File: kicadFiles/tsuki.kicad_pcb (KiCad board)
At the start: 2 copper layers, 283 x 94.2 mm, 392 parts, among them J1 TYPE-C-31-M12_13, J2 Conn_01x12, J3 Conn_ARM_JTAG_SWD_10, Q1 BSS138, Q2 AO4407A, SW1 ESC, SW10 9, SW11 0, SW12 -_, SW13 +=, SW14 2U BKSP, SW15 TAB_150, SW16 Q, SW17 W, SW18 E, SW19 R, SW2 1, SW20 T, SW21 Y, SW22 U, SW23 I, SW24 O, SW25 P, SW26 [{, SW27 ]}, SW28 \|_150, SW29 CAPS_175, SW3 2, SW30 A, SW31 S, SW32 D, SW33 F, SW34 G, SW35 H, SW36 J, SW37 K, SW38 L, SW39 :;, SW4 3, SW40 "', SW41 ENTER_225, SW42 LSHIFT_225, SW43 Z, SW44 X, SW45 C, SW46 V, SW47 B, SW48 N, SW49 M, SW5 4, SW50 <,, SW51 >., SW52 ?/, SW53 RSHIFT_275, SW54 LCTRL_150, SW55 LGUI_100, SW56 LALT_150, SW58 RALT_150, SW59 RGUI_150, SW6 5, SW60 RCTRL_150, SW61 FN_100, SW62 RSHIFT_175, SW63 STEPPED_CAPS_125, SW64 1U LBKSP, SW65 1U RBKSP, SW66 ISO_100, SW67 ISO_ENTER, SW68 LCTRL_125, SW69 LGUI_125, SW7 6, SW70 LGUI_100, SW71 LALT_125, SW72 LALT_150, SW75 SPACE_625, SW77 SPACE_700, SW8 7, SW80 RALT_125, SW81 RALT_150, SW83 RGUI_125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

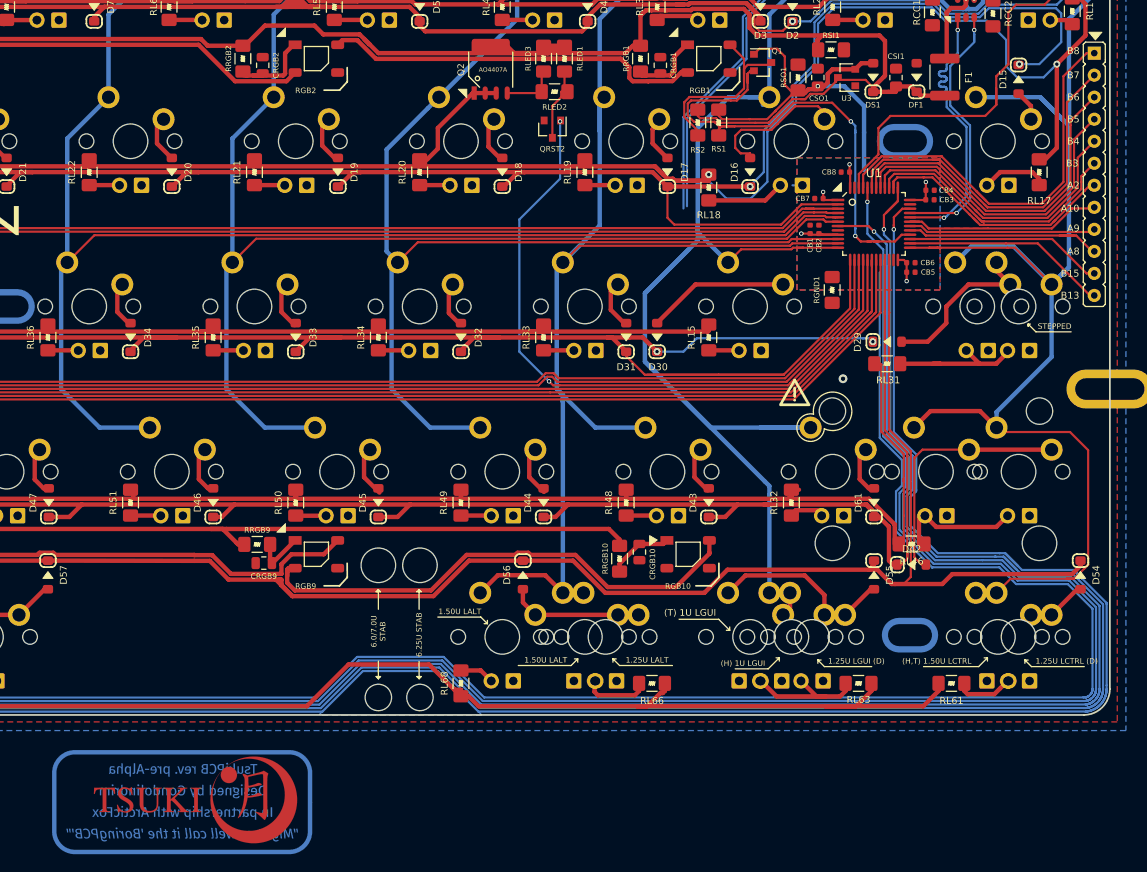
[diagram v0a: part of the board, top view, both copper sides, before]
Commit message: Add rotary encoder support
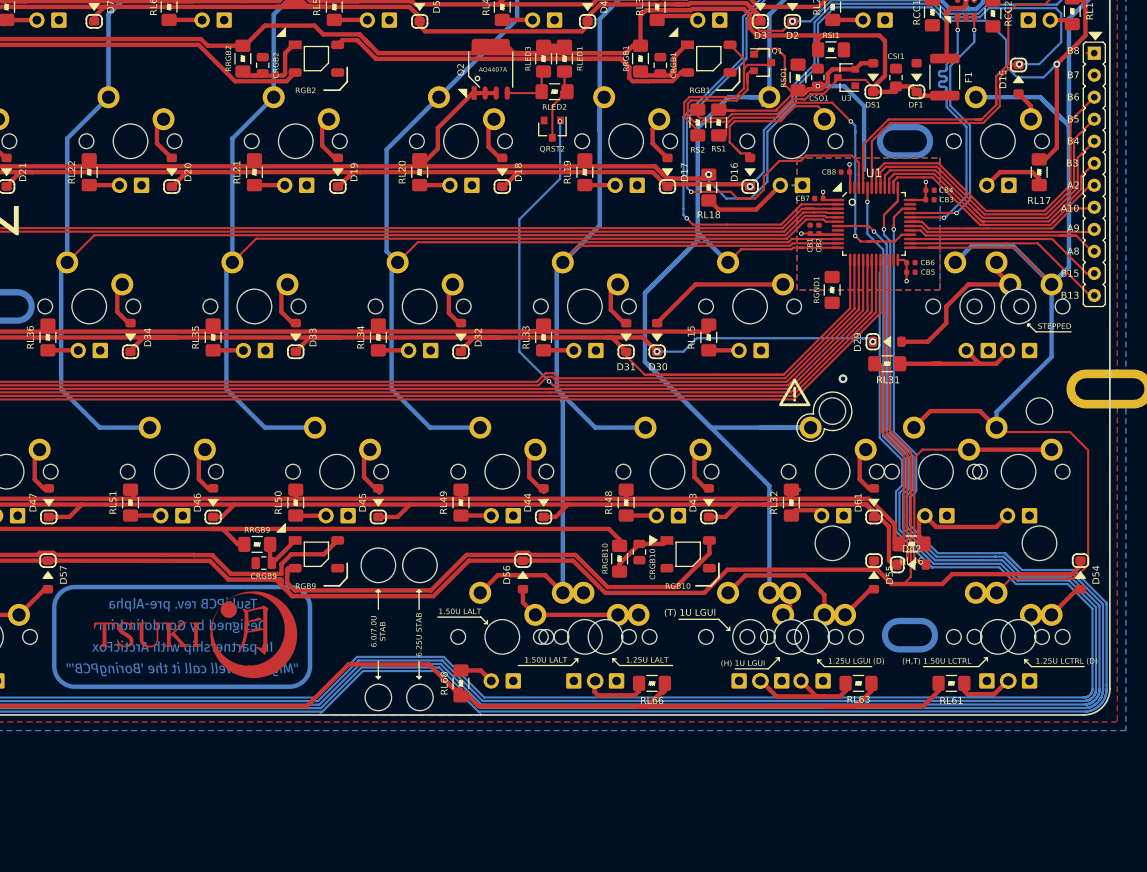
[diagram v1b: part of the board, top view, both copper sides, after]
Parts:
- moved L1 19.1 mm to (248.9, 167.3)
- moved L4 19.1 mm to (247.4, 167.6)
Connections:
- U1 pad 2: Row2 -> ENC_B
- U1 pad 43: Extra2 -> Row2
- U1 pad 45: Extra1 -> Row1
- U1 pad 46: Row1 -> ENC_A
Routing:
- net Extra1: track 47.9 -> 1.52 mm
- net Extra2: track 43.5 -> 0.00 mm
- net ENC_A: track 301.8 -> 326.3 mm, vias 1 -> 2
- net ENC_B: track 305.1 -> 325.1 mm, vias 1 -> 2
- net Row2: track 367.6 -> 371.7 mm
- net Net-(Q2-Pad1): track 1668.3 -> 1664.5 mm
- net Net-(D16-Pad2): track 16.6 -> 19.7 mm
- net RGB_3V3: track 59.4 -> 57.2 mm
- net Net-(LED18-PadA): track 8.98 -> 9.85 mm
- net Row1: track 360.0 -> 360.6 mm
- net 3.3V: track 464.3 -> 464.8 mm

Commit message: Refreshed renders and KLE
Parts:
- removed D66: 1N4148, acheron_Components:D_SOD-123
- removed LED67, LED70: LED, acheron_Components:LED_THT_2.54mm
- removed RL68: 420R, acheron_Components:R_SMD_1206
- removed SW55: LGUI_100, acheron_MX_SolderMask:MX150
- removed SW56: LALT_150, acheron_MX_SolderMask:MX150
- added D63: 1N4148, acheron_Components:D_SOD-123, F.Cu at (117.6, 166.4)
- SW59: value RGUI_150 -> RGUI_100; footprint acheron_MX_SolderMask:MX150 -> acheron_MX_SolderMask:MX100
- moved D59 35.7 mm to (134.2, 160.4)
- moved RLED3 15.3 mm to (273.9, 98.7), turned to 180 degrees
- moved LED77 14.3 mm to (127.1, 172.6)
- moved SW59 14.3 mm to (127.1, 167.6)
- moved RLED2 12.2 mm to (278.9, 100.6), turned to 270 degrees
- moved LED74 9.52 mm to (150.9, 172.6), turned to 180 degrees
- moved SW58 9.52 mm to (150.9, 167.6)
- moved D58 9.52 mm to (143.8, 160.4)
- moved RL71 5.76 mm to (141.6, 173.5)
- moved RL73 5.62 mm to (118.0, 172.8), turned to 270 degrees
- moved L2 3.34 mm to (158.9, 121.7)
- moved RL75 2.73 mm to (115.5, 172.8), turned to 270 degrees
- moved RLED1 2.51 mm to (289.0, 100.5)
- moved LED66 2.38 mm to (317.6, 172.6), turned to 180 degrees
- moved L3 1.09 mm to (208.5, 120.4)
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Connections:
- D58 pad 2: L7 -> L6
- D59 pad 2: L8 -> L7
- LED77 pad A: Net-(LED77-PadA) -> Net-(LED75-PadA)
- LED78 pad A: Net-(LED77-PadA) -> Net-(LED78-PadA)
- LED79 pad A: Net-(LED77-PadA) -> Net-(LED78-PadA)
- Q2 pad 1: Net-(Q2-Pad1) -> 5V
- Q2 pad 2: Net-(Q2-Pad1) -> 5V
- Q2 pad 3: Net-(Q2-Pad1) -> 5V
- Q2 pad 5: 5V -> Net-(Q2-Pad5)
- Q2 pad 6: 5V -> Net-(Q2-Pad5)
- Q2 pad 7: 5V -> Net-(Q2-Pad5)
- Q2 pad 8: 5V -> Net-(Q2-Pad5)
- RL1 pad 2: Net-(Q2-Pad1) -> Net-(Q2-Pad5)
- RL10 pad 2: Net-(Q2-Pad1) -> Net-(Q2-Pad5)
- RL11 pad 2: Net-(Q2-Pad1) -> Net-(Q2-Pad5)
- RL12 pad 2: Net-(Q2-Pad1) -> Net-(Q2-Pad5)
- RL13 pad 2: Net-(Q2-Pad1) -> Net-(Q2-Pad5)
- RL14 pad 2: Net-(Q2-Pad1) -> Net-(Q2-Pad5)
- RL15 pad 2: Net-(Q2-Pad1) -> Net-(Q2-Pad5)
- RL16 pad 2: Net-(Q2-Pad1) -> Net-(Q2-Pad5)
- RL17 pad 2: Net-(Q2-Pad1) -> Net-(Q2-Pad5)
- RL18 pad 2: Net-(Q2-Pad1) -> Net-(Q2-Pad5)
- RL19 pad 2: Net-(Q2-Pad1) -> Net-(Q2-Pad5)
- RL2 pad 2: Net-(Q2-Pad1) -> Net-(Q2-Pad5)
- RL20 pad 2: Net-(Q2-Pad1) -> Net-(Q2-Pad5)
- RL21 pad 2: Net-(Q2-Pad1) -> Net-(Q2-Pad5)
- RL22 pad 2: Net-(Q2-Pad1) -> Net-(Q2-Pad5)
- RL23 pad 2: Net-(Q2-Pad1) -> Net-(Q2-Pad5)
- RL24 pad 2: Net-(Q2-Pad1) -> Net-(Q2-Pad5)
- RL25 pad 2: Net-(Q2-Pad1) -> Net-(Q2-Pad5)
- RL26 pad 2: Net-(Q2-Pad1) -> Net-(Q2-Pad5)
- RL27 pad 2: Net-(Q2-Pad1) -> Net-(Q2-Pad5)
- RL28 pad 2: Net-(Q2-Pad1) -> Net-(Q2-Pad5)
- RL29 pad 2: Net-(Q2-Pad1) -> Net-(Q2-Pad5)
- RL3 pad 2: Net-(Q2-Pad1) -> Net-(Q2-Pad5)
- RL30 pad 2: Net-(Q2-Pad1) -> Net-(Q2-Pad5)
- RL31 pad 2: Net-(Q2-Pad1) -> Net-(Q2-Pad5)
- RL32 pad 2: Net-(Q2-Pad1) -> Net-(Q2-Pad5)
- RL33 pad 2: Net-(Q2-Pad1) -> Net-(Q2-Pad5)
- RL34 pad 2: Net-(Q2-Pad1) -> Net-(Q2-Pad5)
- RL35 pad 2: Net-(Q2-Pad1) -> Net-(Q2-Pad5)
- RL36 pad 2: Net-(Q2-Pad1) -> Net-(Q2-Pad5)
- RL37 pad 2: Net-(Q2-Pad1) -> Net-(Q2-Pad5)
- RL38 pad 2: Net-(Q2-Pad1) -> Net-(Q2-Pad5)
- RL39 pad 2: Net-(Q2-Pad1) -> Net-(Q2-Pad5)
- RL4 pad 2: Net-(Q2-Pad1) -> Net-(Q2-Pad5)
- RL40 pad 2: Net-(Q2-Pad1) -> Net-(Q2-Pad5)
- RL41 pad 2: Net-(Q2-Pad1) -> Net-(Q2-Pad5)
- RL42 pad 2: Net-(Q2-Pad1) -> Net-(Q2-Pad5)
- RL43 pad 2: Net-(Q2-Pad1) -> Net-(Q2-Pad5)
- RL44 pad 2: Net-(Q2-Pad1) -> Net-(Q2-Pad5)
- RL45 pad 2: Net-(Q2-Pad1) -> Net-(Q2-Pad5)
- RL46 pad 2: Net-(Q2-Pad1) -> Net-(Q2-Pad5)
- RL48 pad 2: Net-(Q2-Pad1) -> Net-(Q2-Pad5)
- RL49 pad 2: Net-(Q2-Pad1) -> Net-(Q2-Pad5)
- RL5 pad 2: Net-(Q2-Pad1) -> Net-(Q2-Pad5)
- RL50 pad 2: Net-(Q2-Pad1) -> Net-(Q2-Pad5)
- RL51 pad 2: Net-(Q2-Pad1) -> Net-(Q2-Pad5)
- RL52 pad 2: Net-(Q2-Pad1) -> Net-(Q2-Pad5)
- RL53 pad 2: Net-(Q2-Pad1) -> Net-(Q2-Pad5)
- RL54 pad 2: Net-(Q2-Pad1) -> Net-(Q2-Pad5)
- RL55 pad 2: Net-(Q2-Pad1) -> Net-(Q2-Pad5)
- RL56 pad 2: Net-(Q2-Pad1) -> Net-(Q2-Pad5)
- RL57 pad 2: Net-(Q2-Pad1) -> Net-(Q2-Pad5)
- RL58 pad 2: Net-(Q2-Pad1) -> Net-(Q2-Pad5)
- RL6 pad 2: Net-(Q2-Pad1) -> Net-(Q2-Pad5)
- RL60 pad 2: Net-(Q2-Pad1) -> Net-(Q2-Pad5)
- RL61 pad 2: Net-(Q2-Pad1) -> Net-(Q2-Pad5)
- RL63 pad 2: Net-(Q2-Pad1) -> Net-(Q2-Pad5)
- RL66 pad 2: Net-(Q2-Pad1) -> Net-(Q2-Pad5)
- RL69 pad 2: Net-(Q2-Pad1) -> Net-(Q2-Pad5)
- RL7 pad 2: Net-(Q2-Pad1) -> Net-(Q2-Pad5)
- RL71 pad 2: Net-(Q2-Pad1) -> Net-(Q2-Pad5)
- RL73 pad 2: Net-(Q2-Pad1) -> Net-(Q2-Pad5)
- RL75 pad 1: Net-(LED77-PadA) -> Net-(LED78-PadA)
- RL75 pad 2: Net-(Q2-Pad1) -> Net-(Q2-Pad5)
- RL77 pad 2: Net-(Q2-Pad1) -> Net-(Q2-Pad5)
- RL8 pad 2: Net-(Q2-Pad1) -> Net-(Q2-Pad5)
- RL9 pad 2: Net-(Q2-Pad1) -> Net-(Q2-Pad5)
- SW58 pad 1: Col11 -> Col10
- SW58 pad 2: L7 -> L6
- SW59 pad 1: L8 -> Col11
- SW59 pad 2: Col12 -> L7
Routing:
- net Net-(Q2-Pad1): track 1664.5 -> 0.00 mm, vias 2 -> 0
- net Net-(Q2-Pad5): track 0.00 -> 1653.5 mm, vias 0 -> 2
- net Net-(LED77-PadA): track 16.2 -> 0.00 mm
- net L2: track 22.1 -> 6.94 mm
- net Col3: track 145.4 -> 134.2 mm
- net Net-(QRST2-Pad3): track 8.92 -> 18.5 mm
- net Net-(LED78-PadA): track 0.00 -> 9.34 mm
- net Net-(LED65-PadA): track 15.2 -> 7.01 mm
- net Net-(LED75-PadA): track 7.71 -> 15.3 mm
- net L8: track 16.2 -> 8.78 mm
- net Net-(LED73-PadA): track 17.5 -> 10.3 mm
- net L7: track 15.3 -> 10.5 mm
- net L6: track 12.5 -> 16.9 mm
- net Net-(LED70-PadA): track 3.99 -> 0.00 mm
- net Row5: track 327.0 -> 330.5 mm
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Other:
- board text added: "(H) 1U RGUI"
- board text added: "(H,T) 1.50U LALT"
- board text added: "(H,T) 1U LGUI"
- board text added: "(IV) For detailed information, check the Acheron Docs page for the ArcticPCB: http://gondolindrim.github.io/AcheronDocs/tsuki/intro.html"
- board text added: "(T) 1.50U LCTRL"
- board text added: "- TsukiPCB's GitHub page: http://github.com/Gondolindrim/TsukiPCB"
- board text added: "1.50U RALT (T)"
- board text removed: "(H) 1U LGUI"
- board text removed: "(H,T) 1.50U LCTRL"
- board text removed: "(IV) For detailed information, check the Acheron Docs page for the ArcticPCB: http://gondolindrim.github.io/AcheronDocs/arctic/intro.html"
- board text removed: "(T) 1.50U RALT"
- board text removed: "(T) 1U LGUI"
- board text removed: "- ArcticPCB's GitHub page: http://github.com/Gondolindrim/ArcticPCB"
- board text removed: "1.50U LALT"
- board text removed: "1.50U RGUI (H)"

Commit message: Further adjust schematic
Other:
- board text removed: "(vi) Some switch fooprints had to be"
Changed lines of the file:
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@@
   (general
     (thickness 1.6)
-    (drawings 247)
+    (drawings 246)
     (tracks 2920)
     (zones 0)
@@
     (title Tsuki)
     (date 2019-09-26)
-    (rev 0.1)
+    (rev pre-Alpha)
     (comment 1 "Designed by Gondolindrim")
-    (comment 2 "Project page: http://github.com/Gondolindrim/Tsuki60")
+    (comment 2 "Project page: http://github.com/Gondolindrim/Tsuki")
   )
   (layers
@@
     (36 B.SilkS user)
     (37 F.SilkS user)
-    (38 B.Mask user)
+    (38 B.Mask user hide)
     (39 F.Mask user)
     (40 Dwgs.User user)
-    (41 Cmts.User user hide)
+    (41 Cmts.User user)
     (42 Eco1.User user hide)
     (43 Eco2.User user hide)
@@
   )
   (setup
-    (last_trace_width 0.508)
+    (last_trace_width 0.1524)
     (user_trace_width 0.1524)
     (user_trace_width 0.254)
@@
     (effects (font (size 0.762 0.762) (thickness 0.1524)))
   )
-  (gr_text "(vi) Some switch fooprints had to be " (at 422.37625 271.693125) (layer Cmts.User)
-    (effects (font (size 1.524 1.524) (thickness 0.1524)) (justify left))
-  )
   (gr_text "(IV) For detailed information, check the Acheron Docs page for the ArcticPCB:\nhttp://gondolindrim.github.io/AcheronDocs/tsuki/intro.html" (at 419.83625 87.543125) (layer Cmts.User)
     (effects (font (size 1.524 1.524) (thickness 0.1524)) (justify left))
@@
   (segment (start 129.392 171.272625) (end 130.7525 172.633125) (width 0.508) (layer F.Cu) (net 206))
   (segment (start 124.46951 171.272625) (end 129.392 171.272625) (width 0.508) (layer F.Cu) (net 206))
-  (segment (start 106.94 172.633125) (end 108.718 170.855125) (width 0.508) (layer F.Cu) (net 215))
-  (segment (start 108.718 170.855125) (end 115.54425 170.855125) (width 0.508) (layer F.Cu) (net 215))
   (segment (start 82.96875 172.633125) (end 84.87375 170.728125) (width 0.508) (layer F.Cu) (net 207))
   (segment (start 84.87375 170.728125) (end 86.84225 170.728125) (width 0.508) (layer F.Cu) (net 207))
@@
   (segment (start 117.95725 174.247625) (end 117.95725 175.490625) (width 0.508) (layer F.Cu) (net 214))
   (segment (start 115.54425 174.247625) (end 115.54425 175.490625) (width 0.508) (layer F.Cu) (net 214))
+  (segment (start 106.94 172.633125) (end 108.718 170.855125) (width 0.508) (layer F.Cu) (net 215))
+  (segment (start 108.718 170.855125) (end 115.54425 170.855125) (width 0.508) (layer F.Cu) (net 215))
   (zone (net 0) (net_name "") (layer F.Cu) (hatch edge 0.508)
     (connect_pads (clearance 0.508))
